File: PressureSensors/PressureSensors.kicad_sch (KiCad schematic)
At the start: 27 parts, among them IC1 BD733L2FP3-CE2, J1 Conn_02x03_Odd_Even, U1 LPS22HB, U2 LPS22HB, U3 LPS22HB, U4 LPS22HB, U5 PCA9543AD

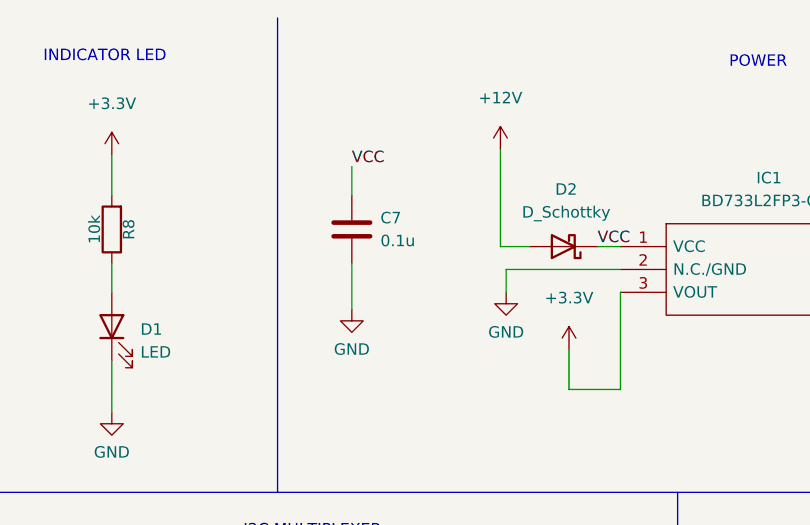
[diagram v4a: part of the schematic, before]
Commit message: Changed power source capacitor from 0.1u to 1u
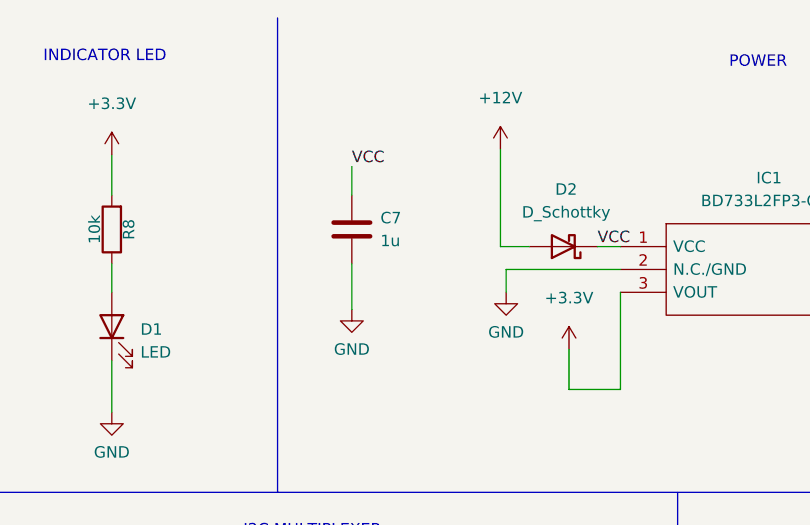
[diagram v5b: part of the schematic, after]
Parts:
- C7: value 0.1u -> 1u
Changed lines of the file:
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@@
       (effects (font (size 1.27 1.27)) (justify left))
     )
-    (property "Value" "0.1u" (id 1) (at 193.04 36.8299 0)
+    (property "Value" "1u" (id 1) (at 193.04 36.8299 0)
       (effects (font (size 1.27 1.27)) (justify left))
     )
@@
     )
     (path "/dfda87cb-0ac8-4831-aebf-0d999d9fa492"
-      (reference "C7") (unit 1) (value "0.1u") (footprint "Capacitor_SMD:C_0805_2012Metric_Pad1.18x1.45mm_HandSolder")
+      (reference "C7") (unit 1) (value "1u") (footprint "Capacitor_SMD:C_0805_2012Metric_Pad1.18x1.45mm_HandSolder")
     )
     (path "/c09022ea-afac-415b-a921-4dcd47fbfb9e"
